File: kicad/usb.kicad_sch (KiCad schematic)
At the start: 24 parts, among them U10 TPD4EUSB30DQAR-N, U13 AP22653W6-7, U4 FSUSB42MUX, U9 USB2514B-I/M2, X2 X322524MOB4SI

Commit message: CM4 schematic changes, before renumbering
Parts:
- removed C80: 100uF, Capacitor_Tantalum_SMD:CP_EIA-7343-31_Kemet-D, symbol Device:CP
- removed C85, C86: 22pF, PCM_JLCPCB:C_0402, symbol PCM_JLCPCB-Capacitors:0402,22pF
- added C80: 100uF 6.3V, Capacitor_Tantalum_SMD:CP_EIA-7343-31_Kemet-D, symbol Device:C_Polarized
- added C85, C86: 15pF, PCM_JLCPCB:C_0402, symbol PCM_JLCPCB-Capacitors:0402,15pF
- added R94: 2.2kΩ, MyParts:R0402, symbol PCM_JLCPCB-Resistors:0402,2.2kΩ
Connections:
- net GND: now also C80.2, C85.2, C86.2
- net USB_OTG_ID: now also R94.1
- net VBUS: now also C80.1; no longer USBC1.A4B9 (VBUS), USBC1.B4A9 (VBUS)
- net nEXTRST: now also U9.26 (RESET_N); no longer U9.11 (TEST)
- net at U9.33 (XTALIN/CLKIN), X2.1 (OSC1): now also C85.1
- net at U9.32 (XTALOUT), X2.3 (OSC2): now also C86.1
- new net: R94.2, USBC1.A4B9 (VBUS), USBC1.B4A9 (VBUS)
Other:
- moved on the sheet: U10

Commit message: Before adding CAN
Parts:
- renumbered C109 to C81, C80 to C82, C92 to C83, C93 to C84, C94 to C85, C108 to C86, C86 to C87, C85 to C88, R94 to R81, R23 to R82, R89 to R83, R90 to R84, R88 to R85, R87 to R86, R83 to R87, R84 to R88, R85 to R89, R86 to R90, U13 to U11, U10 to U12, U4 to U13, U9 to U14

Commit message: More mods
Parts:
- added D36: SMF6.0A, PCM_JLCPCB:D_SOD-123FL, symbol PCM_JLCPCB-Diodes:TVS-Uni,SMF6.0A
- added U21: TPD4EUSB30DQAR-N, MyParts:DFN-10_L2.5-W1.0-P0.50-BL-A, symbol MyParts:TPD4EUSB30DQAR-N
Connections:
- net GND: now also D36.2, U21.3, U21.8
- net HD1_N: now also U21.5
- net HD1_P: now also U21.4
- net HD2_N: now also U21.2
- net HD2_P: now also U21.1
- net VBUS: now also D36.1
- no-connect marks 18 -> 22
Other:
- note added: "U21 protects both USB-A ports (4 lines). D36 clamps VBUS. Place both at USB1."

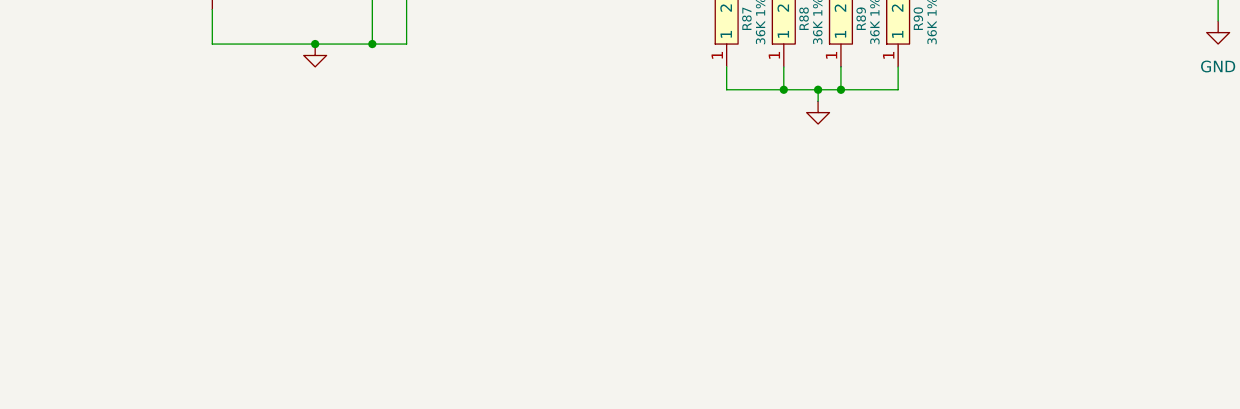
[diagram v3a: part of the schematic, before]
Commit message: Part positioning of PWR, USB, Ethernet
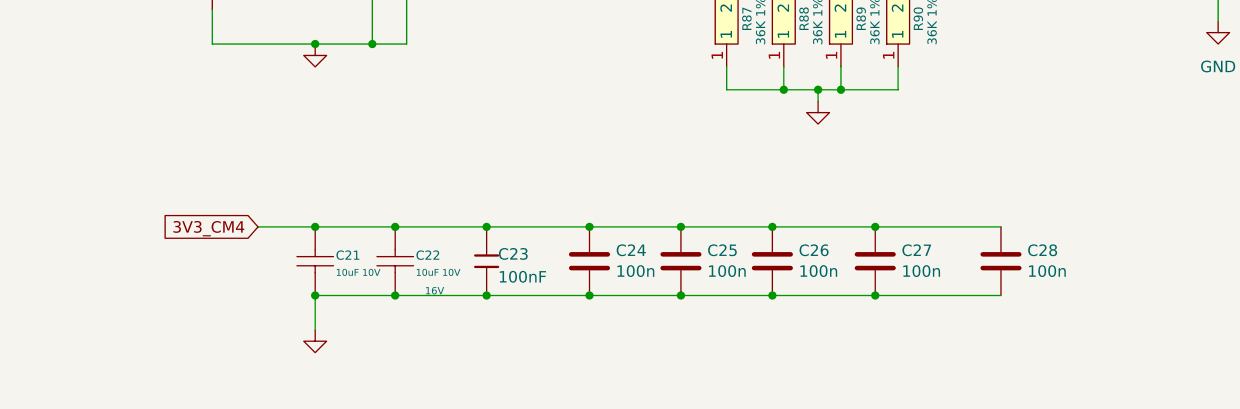
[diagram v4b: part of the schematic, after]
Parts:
- added C21, C22: 10uF 10V, MyParts:C0805, symbol MyParts:CL21B106KPQNNNE
- added C23: 100nF, PCM_JLCPCB:C_0402, symbol PCM_JLCPCB-Capacitors:0402,100nF
- added C24, C25, C26, C27, C28: 100n, Capacitor_SMD:C_0402_1005Metric, symbol Device:C
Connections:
- net 3V3_CM4: now also C21.2, C22.2, C23.1, C24.1, C25.1, C26.1, C27.1, C28.1
- net GND: now also C21.1, C22.1, C23.2, C24.2, C25.2, C26.2, C27.2, C28.2

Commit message: CAN looks complete in schematic
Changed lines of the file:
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@@
 			)
 		)
-		(property "Description" ""
+		(property "Description" "Unpolarized capacitor"
 			(at 93.98 170.18 0)
 			(show_name no)
@@
 			)
 		)
-		(property "Description" ""
+		(property "Description" "Unpolarized capacitor"
 			(at 104.14 170.18 0)
 			(show_name no)
@@
 			)
 		)
-		(property "Description" ""
+		(property "Description" "Unpolarized capacitor"
 			(at 129.54 170.18 0)
 			(show_name no)
@@
 			)
 		)
-		(property "Description" ""
+		(property "Description" "Unpolarized capacitor"
 			(at 115.57 170.18 0)
 			(show_name no)
@@
 			)
 		)
-		(property "Description" ""
+		(property "Description" "Unpolarized capacitor"
 			(at 83.82 170.18 0)
 			(show_name no)

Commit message: Add CAN JR45 - still working on it
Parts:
- renumbered C81 to C69, C82 to C70, C83 to C71, C84 to C72, C85 to C73, C86 to C74, C87 to C75, C88 to C76, C21 to C77, C22 to C78, C23 to C79, C24 to C80, C25 to C81, C26 to C82, C27 to C83, C28 to C84, D36 to D39, U11 to U10, U12 to U11, U13 to U12, U14 to U13, U21 to U14
